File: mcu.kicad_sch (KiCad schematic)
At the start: 32 parts, among them J8 Conn_ARM_SWD_TagConnect_TC203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, J9 Conn_01x05_Pin, SW2 Reset, U1 nRF52840-QIAA, X1 32MHz, X2 32.768kHz

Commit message: Sorting out other pads and sensor voltage jumper
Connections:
- net PlanB 1: now also U1.R1 (P1.09)
- net PlanB 2: now also U1.N1 (P0.08)
- net PlanB 3: now also U1.L1 (P0.06)
- net PlanB 4: now also U1.J1 (P0.04/AIN2)
- net PlanB 5: now also U1.G1 (P0.26)

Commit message: Wiring the columns socket
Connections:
- net Col 0: now also U1.AC9 (P0.14)
- net Col 1: now also U1.AC11 (P0.16)
- net Col 2: now also U1.AD16 (P0.20)
- net Col 3: now also U1.AD18 (P0.22)
- net Col 4: now also U1.AD20 (P0.24)
- net Col 5: now also U1.AD22 (P1.00)
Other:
- moved on the sheet: C7

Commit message: Swapping rows connector to the same 6 pins as columns
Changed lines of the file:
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@@
+		)
+	)
+	(hierarchical_label "Row 5"
+		(shape input)
+		(at 135.89 172.72 270)
+		(effects
+			(font
+				(size 1.27 1.27)
+			)
+			(justify right)
 		)
 	)
@@
 					(unit 1)
 				)
+			)
+		)
+	)
+	(symbol
+		(lib_id "npm1100_caax_config1-altium-import:VBUS_BAR")
+		(at 135.89 172.72 180)
+		(unit 1)
+		(exclude_from_sim no)
+		(in_bom yes)
+		(on_board yes)
+		(dnp no)
+		(property "Reference" "#PWR073"
+			(at 135.89 172.72 0)
+			(effects
+				(font
+					(size 1.27 1.27)
+				)
+				(hide yes)
+			)
+		)
+		(property "Value" "Row 5"
+			(at 135.89 164.338 90)
+			(effects
+				(font
+					(size 1.27 1.27)
+				)
+			)
+		)
+		(property "Footprint" ""
+			(at 135.89 172.72 0)
+			(effects
+				(font
+					(size 1.27 1.27)
+				)
+			)
+		)
+		(property "Datasheet" ""
+			(at 135.89 172.72 0)
+			(effects
+				(font
+					(size 1.27 1.27)
+				)
+			)
+		)
+		(property "Description" ""
+			(at 135.89 172.72 0)
+			(effects
+				(font
+					(size 1.27 1.27)
+				)
+			)
+		)
+		(pin ""
+		)
+		(instances
+			(project "plan-b"
+				(path "/3a835e6f-a660-4b38-a102-87841cdd95ed/5bb1d2f7-c8fd-447b-99e1-d61ef924696c"
+					(reference "#PWR073")
+					(unit 1)
+				)

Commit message: Wiring the rows connector to the MCU
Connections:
- net BLED: now also U1.AC21 (P0.25)
- net Col 0: now also U1.AC15 (P0.19); no longer U1.AC9 (P0.14)
- net Col 1: now also U1.AC17 (P0.21); no longer U1.AC11 (P0.16)
- net Row 0: now also U1.U1 (P0.12)
- net Row 1: now also U1.T2 (P0.11)
- net Row 2: now also U1.P2 (P1.08)
- net Row 3: now also U1.M2 (P0.07)
- net Row 4: now also U1.AC9 (P0.14)
- net Row 5: now also U1.AC11 (P0.16)

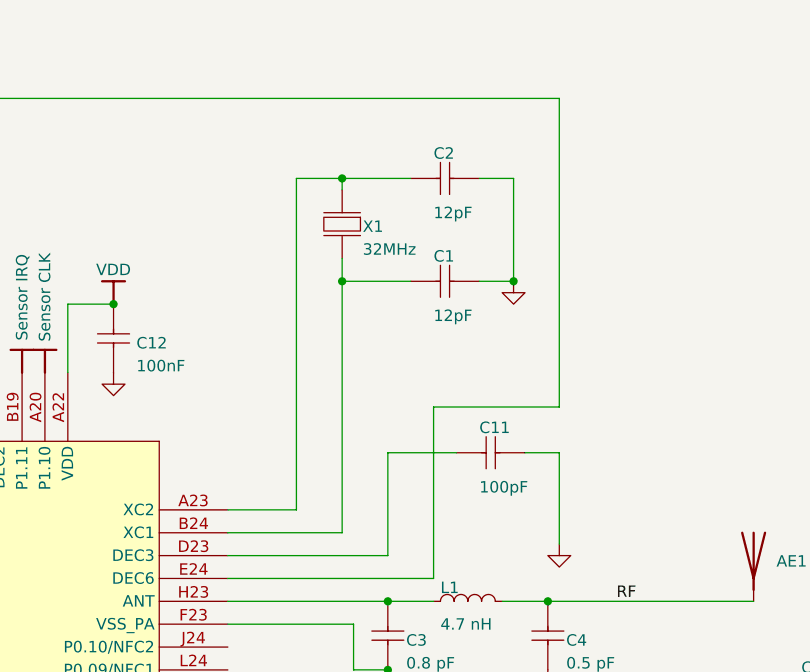
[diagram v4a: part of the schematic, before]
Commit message: Sorting out the GND fills
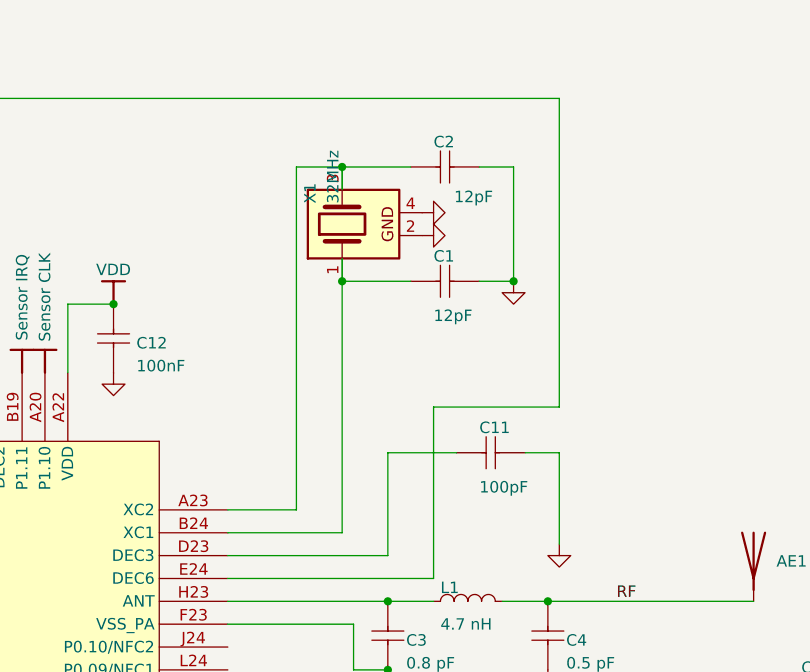
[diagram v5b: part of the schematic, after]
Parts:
- X1: symbol AltiumLib:root_1_XTAL_4-pin_grounded_AltiumLib.DbLib -> PCM_Crystal_AKL:Crystal_Generic_GND24
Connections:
- net GND: now also X1.2, X1.4
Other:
- moved on the sheet: C2
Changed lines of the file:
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@@
 	)
 	(junction
+		(at 190.5 38.1)
+		(diameter 0)
+		(color 0 0 0 0)
+	)
+	(junction
 		(at 213.36 86.36)
 		(diameter 0)
@@
 	)
 	(junction
-		(at 190.5 39.37)
-		(diameter 0)
-		(color 0 0 0 0)
-	)
-	(junction
 		(at 128.27 30.48)
 		(diameter 0)
@@
 	(wire
 		(pts
-			(xy 190.5 39.37) (xy 190.5 40.64)
+			(xy 190.5 38.1) (xy 190.5 40.64)
 		)
 		(stroke
@@
 	(wire
 		(pts
-			(xy 209.55 39.37) (xy 205.74 39.37)
+			(xy 209.55 38.1) (xy 205.74 38.1)
 		)
 		(stroke
@@
 	(wire
 		(pts
-			(xy 185.42 39.37) (xy 190.5 39.37)
+			(xy 185.42 38.1) (xy 190.5 38.1)
 		)
 		(stroke
@@
 	(wire
 		(pts
+			(xy 190.5 50.8) (xy 190.5 78.74)
+		)
+		(stroke
+			(width 0)
+			(type default)
+		)
+	)
+	(wire
+		(pts
 			(xy 177.8 76.2) (xy 185.42 76.2)
 		)
@@
 	(wire
 		(pts
-			(xy 190.5 39.37) (xy 198.12 39.37)
+			(xy 190.5 38.1) (xy 198.12 38.1)
 		)
 		(stroke
@@
 	(wire
 		(pts
-			(xy 190.5 50.8) (xy 190.5 78.74)
-		)
-		(stroke
-			(width 0)
-			(type default)
-		)
-	)
-	(wire
-		(pts
 			(xy 177.8 81.28) (xy 195.58 81.28)
 		)
@@
 	(wire
 		(pts
-			(xy 209.55 50.8) (xy 209.55 39.37)
+			(xy 209.55 50.8) (xy 209.55 38.1)
 		)
 		(stroke
@@
 	(wire
 		(pts
-			(xy 185.42 76.2) (xy 185.42 39.37)
+			(xy 185.42 76.2) (xy 185.42 38.1)
 		)
 		(stroke
@@
 	)
 	(symbol
+		(lib_id "power:GND")
+		(at 199.39 43.18 90)
+		(unit 1)
+		(exclude_from_sim no)
+		(in_bom yes)
+		(on_board yes)
+		(dnp no)
+		(property "Reference" "#PWR0119"
+			(at 205.74 43.18 0)
+			(effects
+				(font
+					(size 1.27 1.27)
+				)
+				(hide yes)
+			)
+		)
+		(property "Value" "GND"
+			(at 203.962 45.212 0)
+			(effects
+				(font
+					(size 1.27 1.27)
+				)
+				(justify left)
+				(hide yes)
+			)
+		)
+		(property "Footprint" ""
+			(at 199.39 43.18 0)
+			(effects
+				(font
+					(size 1.27 1.27)
+				)
+				(hide yes)
+			)
+		)
+		(property "Datasheet" ""
+			(at 199.39 43.18 0)
+			(effects
+				(font
+					(size 1.27 1.27)
+				)
+				(hide yes)
+			)
+		)
+		(property "Description" "Power symbol creates a global label with name \"GND\" , ground"
+			(at 199.39 43.18 0)
+			(effects
+				(font
+					(size 1.27 1.27)
+				)
+				(hide yes)
+			)
+		)
+		(pin "1"
+		)
+		(instances
+			(project "plan-b"
+				(path "/3a835e6f-a660-4b38-a102-87841cdd95ed/5bb1d2f7-c8fd-447b-99e1-d61ef924696c"
+					(reference "#PWR0119")
+					(unit 1)
+				)
+			)
+		)
+	)
+	(symbol
 		(lib_id "npm1100_caax_config1-altium-import:VBUS_BAR")
 		(at 134.62 139.7 0)
@@
 	)
 	(symbol
-		(lib_id "AltiumLib:root_1_XTAL_4-pin_grounded_AltiumLib.DbLib")
-		(at 190.5 48.26 0)
+		(lib_id "PCM_Crystal_AKL:Crystal_Generic_GND24")
+		(at 190.5 44.45 90)
 		(unit 1)
 		(exclude_from_sim no)
@@
 		(dnp no)
 		(property "Reference" "X1"
-			(at 192.786 45.466 0)
+			(at 187.706 42.164 0)
 			(effects
 				(font
@@
 		)
 		(property "Value" "32MHz"
-			(at 192.786 48.006 0)
+			(at 190.246 42.164 0)
 			(effects
 				(font
@@
 		)
 		(property "Footprint" "NX1612SA-32.000MHZ-CHP:OSCSC105P160X120X35-4N"
-			(at 190.5 48.26 0)
+			(at 190.5 44.45 0)
 			(effects
 				(font
@@
 			)
 		)
-		(property "Datasheet" ""
-			(at 190.5 48.26 0)
+		(property "Datasheet" "~"
+			(at 190.5 44.45 0)
 			(effects
 				(font
@@
 			)
 		)
-		(property "Description" "XTAL SMD 2016, 32MHz, Cl=8pF, Total Tol: ±40ppm"
-			(at 190.5 48.26 0)
+		(property "Description" "Quartz crystal, Shielded, Generic symbol, Alternate KiCad Library"
+			(at 190.5 44.45 0)
 			(effects
 				(font
@@
 		)
 		(property "PART NUMBER" "XTAL_SMD2016_32MHz_8pF_General"
-			(at 189.992 40.64 0)
+			(at 182.88 44.958 0)
 			(effects
 				(font
@@
 		)
 		(property "LATESTREVISIONDATE" "2016-08-19"
-			(at 189.992 38.1 0)
+			(at 180.34 44.958 0)
 			(effects
 				(font
@@
 		)
 		(property "PAD COUNT" "4"
-			(at 189.992 38.1 0)
+			(at 180.34 44.958 0)
 			(effects
 				(font
@@
 		)
 		(property "PUBLISHED" "2016-08-19"
-			(at 189.992 38.1 0)
+			(at 180.34 44.958 0)
 			(effects
 				(font
@@
 		)
 		(property "ALTIUM_VALUE" "32MHz"
-			(at 189.992 38.1 0)
+			(at 180.34 44.958 0)
 			(effects
 				(font
@@
 		)
 		(property "FOOTPRINT DOC" "XTAL_2016"
-			(at 189.992 38.1 0)
+			(at 180.34 44.958 0)
 			(effects
 				(font
@@
 		)
 		(property "ASSEMBLY" ""
-			(at 192.786 50.546 0)
+			(at 192.786 42.164 0)
 			(effects
 				(font
@@
 		)
 		(property "AUTHOR" ""
-			(at 188.214 40.132 0)
+			(at 182.372 46.736 0)
 			(effects
 				(font
@@
 	)
 	(symbol
+		(lib_id "power:GND")
+		(at 199.39 45.72 90)
+		(unit 1)
+		(exclude_from_sim no)
+		(in_bom yes)
+		(on_board yes)
+		(dnp no)
+		(property "Reference" "#PWR0118"
+			(at 205.74 45.72 0)
+			(effects
+				(font
+					(size 1.27 1.27)
+				)
+				(hide yes)
+			)
+		)
+		(property "Value" "GND"
+			(at 203.962 47.752 0)
+			(effects
+				(font
+					(size 1.27 1.27)
+				)
+				(justify left)
+				(hide yes)
+			)
+		)
+		(property "Footprint" ""
+			(at 199.39 45.72 0)
+			(effects
+				(font
+					(size 1.27 1.27)
+				)
+				(hide yes)
+			)
+		)
+		(property "Datasheet" ""
+			(at 199.39 45.72 0)
+			(effects
+				(font
+					(size 1.27 1.27)
+				)
+				(hide yes)
+			)
+		)
+		(property "Description" "Power symbol creates a global label with name \"GND\" , ground"
+			(at 199.39 45.72 0)
+			(effects
+				(font
+					(size 1.27 1.27)
+				)
+				(hide yes)
+			)
+		)
+		(pin "1"
+		)
+		(instances
+			(project "plan-b"
+				(path "/3a835e6f-a660-4b38-a102-87841cdd95ed/5bb1d2f7-c8fd-447b-99e1-d61ef924696c"
+					(reference "#PWR0118")
+					(unit 1)
+				)
+			)
+		)
+	)
+	(symbol
 		(lib_id "npm1100_caax_config1-altium-import:VOUT_BAR")
 		(at 127 60.96 180)
@@
 	(symbol
 		(lib_id "AltiumLib:root_0_CAP_AltiumLib.DbLib")
-		(at 198.12 39.37 0)
+		(at 198.12 38.1 0)
 		(unit 1)
 		(exclude_from_sim no)
@@
 		(dnp no)
 		(property "Reference" "C2"
-			(at 200.66 37.338 0)
+			(at 200.66 36.068 0)
 			(effects
 				(font
@@
 		)
 		(property "Value" "12pF"
-			(at 200.66 43.942 0)
+			(at 202.946 42.164 0)
 			(effects
 				(font
@@
 		)
 		(property "Footprint" "Library:C_0402_1005"
-			(at 198.12 39.37 0)
+			(at 198.12 38.1 0)
 			(effects
 				(font
@@
 		)
 		(property "Datasheet" ""
-			(at 198.12 39.37 0)
+			(at 198.12 38.1 0)
 			(effects
 				(font
@@
 		)
 		(property "Description" "Capacitor, NP0, ±2%"
-			(at 198.12 39.37 0)
+			(at 198.12 38.1 0)
 			(effects
 				(font
@@
 		)
 		(property "PART NUMBER" "C0402-12p"
-			(at 197.612 37.338 0)
+			(at 197.612 36.068 0)
 			(effects
 				(font
@@
 		)
 		(property "LATESTREVISIONDATE" "2011-05-11"
-			(at 197.612 37.338 0)
+			(at 197.612 36.068 0)
 			(effects
 				(font
@@
 		)
 		(property "PAD COUNT" "2"
-			(at 197.612 37.338 0)
+			(at 197.612 36.068 0)
 			(effects
 				(font
@@
 		)
 		(property "PUBLISHED" "2009-05-08"
-			(at 197.612 37.338 0)
+			(at 197.612 36.068 0)
 			(effects
 				(font
@@
 		)
 		(property "ALTIUM_VALUE" "12pF"
-			(at 197.612 37.338 0)
+			(at 197.612 36.068 0)
 			(effects
 				(font
@@
 		)
 		(property "FOOTPRINT DOC" "0402"
-			(at 197.612 37.338 0)
+			(at 197.612 36.068 0)
 			(effects
 				(font
@@
 		)
 		(property "ASSEMBLY" ""
-			(at 197.612 34.798 0)
+			(at 197.612 33.528 0)
 			(effects
 				(font
@@
 		)
 		(property "AUTHOR" ""
-			(at 197.612 34.798 0)
+			(at 197.612 33.528 0)
 			(effects
 				(font

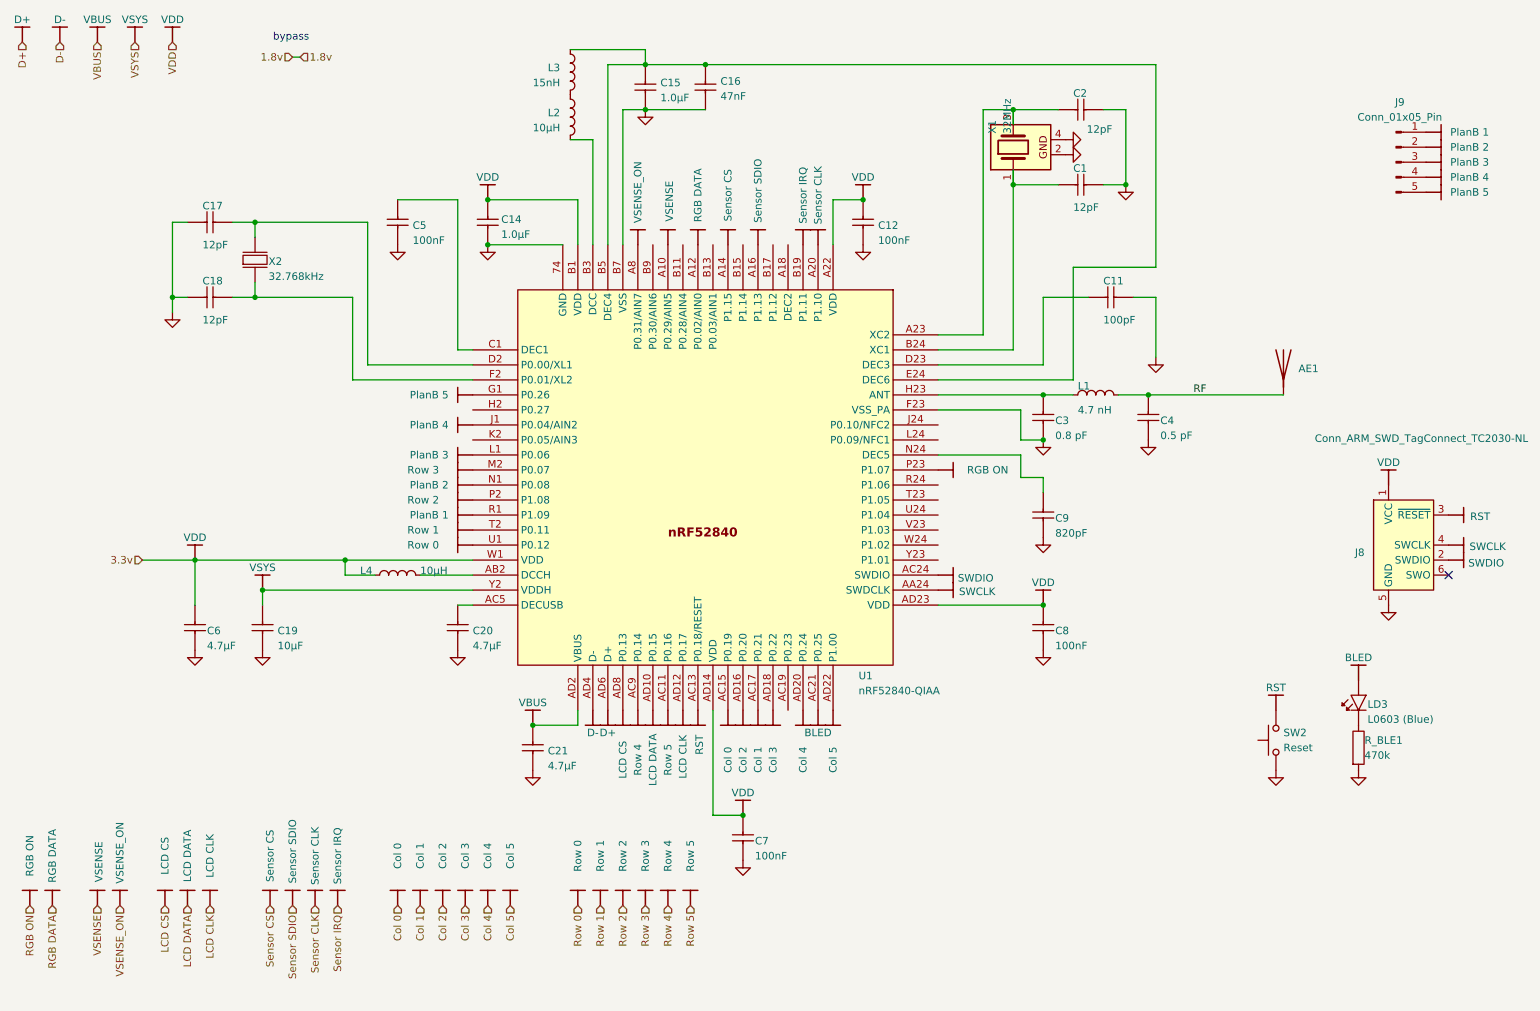
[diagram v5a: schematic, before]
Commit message: Optimising for BOM and placements cost reduction
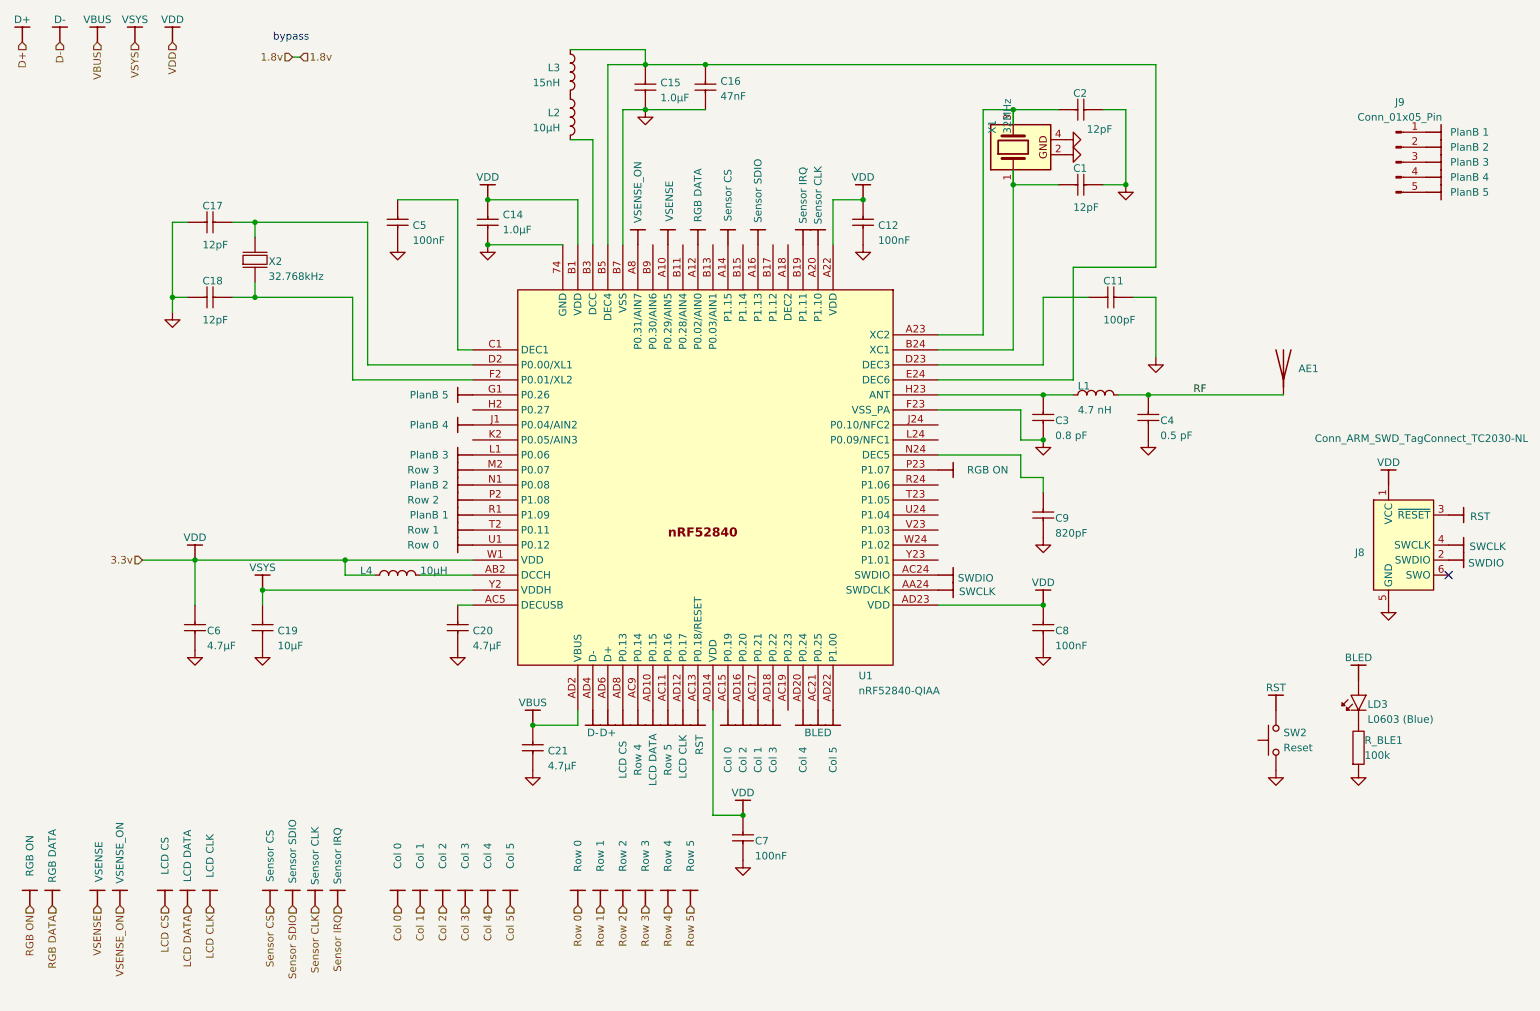
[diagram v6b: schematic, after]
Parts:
- C14, C15: footprint Library:C_0603_1608 -> Library:C_0402_1005
- R_BLE1: value 470k -> 100k
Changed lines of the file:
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@@
 		(on_board yes)
 		(dnp no)
+		(fields_autoplaced yes)
 		(property "Reference" "C14"
-			(at 103.886 57.404 0)
+			(at 104.14 55.8799 0)
 			(effects
 				(font
 					(size 1.27 1.27)
 				)
-				(justify left bottom)
+				(justify left)
 			)
 		)
 		(property "Value" "1.0µF"
-			(at 103.886 59.944 0)
+			(at 104.14 58.4199 0)
 			(effects
 				(font
 					(size 1.27 1.27)
 				)
-				(justify left bottom)
+				(justify left)
 			)
 		)
-		(property "Footprint" "Library:C_0603_1608"
+		(property "Footprint" "Library:C_0402_1005"
 			(at 101.6 53.34 0)
 			(effects
@@
 			)
 		)
-		(property "Value" "470k"
+		(property "Value" "100k"
 			(at 249.936 148.082 0)
 			(effects
@@
 			)
 		)
-		(property "Footprint" "Library:C_0603_1608"
+		(property "Footprint" "Library:C_0402_1005"
 			(at 128.27 38.1 0)
 			(effects

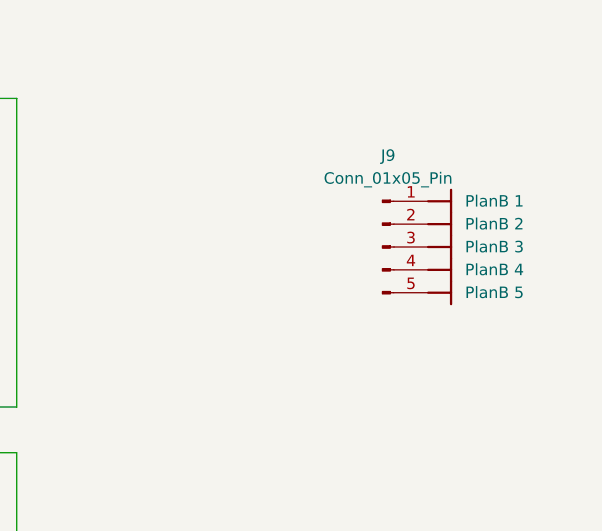
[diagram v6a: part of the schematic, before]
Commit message: Further optimising the BOM and adding JLCPCB specific part numbers
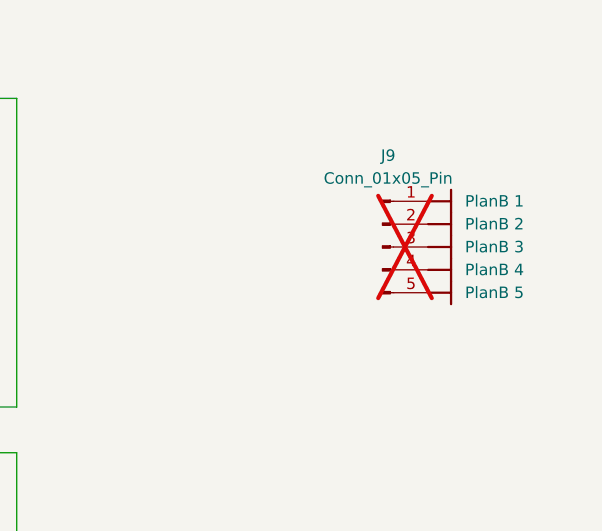
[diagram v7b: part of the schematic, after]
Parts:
- AE1: value 2450AT18A100E -> ANT2012LL13R2400A; LCSC (none) -> C19192917; MF Johanson Technology -> (none)
- C1, C17, C18, C2: LCSC (none) -> C1547
- C11: LCSC (none) -> C1546
- C12, C5, C7, C8: LCSC (none) -> C1525
- C14, C15: LCSC (none) -> C52923
- C16: LCSC (none) -> C82219
- C19: LCSC (none) -> C19702
- C20, C21, C6: LCSC (none) -> C1624
- C3: LCSC (none) -> C40459
- C4: LCSC (none) -> C76912
- C9: LCSC (none) -> C107031
- J9: now not fitted; now left out of the parts list
- L1: LCSC (none) -> C86065
- L2, L4: LCSC (none) -> C1035
- L3: LCSC (none) -> C86059
- LD3: LCSC (none) -> C84266
- R_BLE1: LCSC (none) -> C25741
- SW2: LCSC (none) -> C963349
- U1: LCSC (none) -> C1851953
- X1: LCSC (none) -> C910049
- X2: LCSC (none) -> C5682932
